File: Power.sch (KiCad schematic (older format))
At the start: 38 parts, among them J17 Power Input, Q4 YJS9435A, U6 A4403, U7 MCP16301

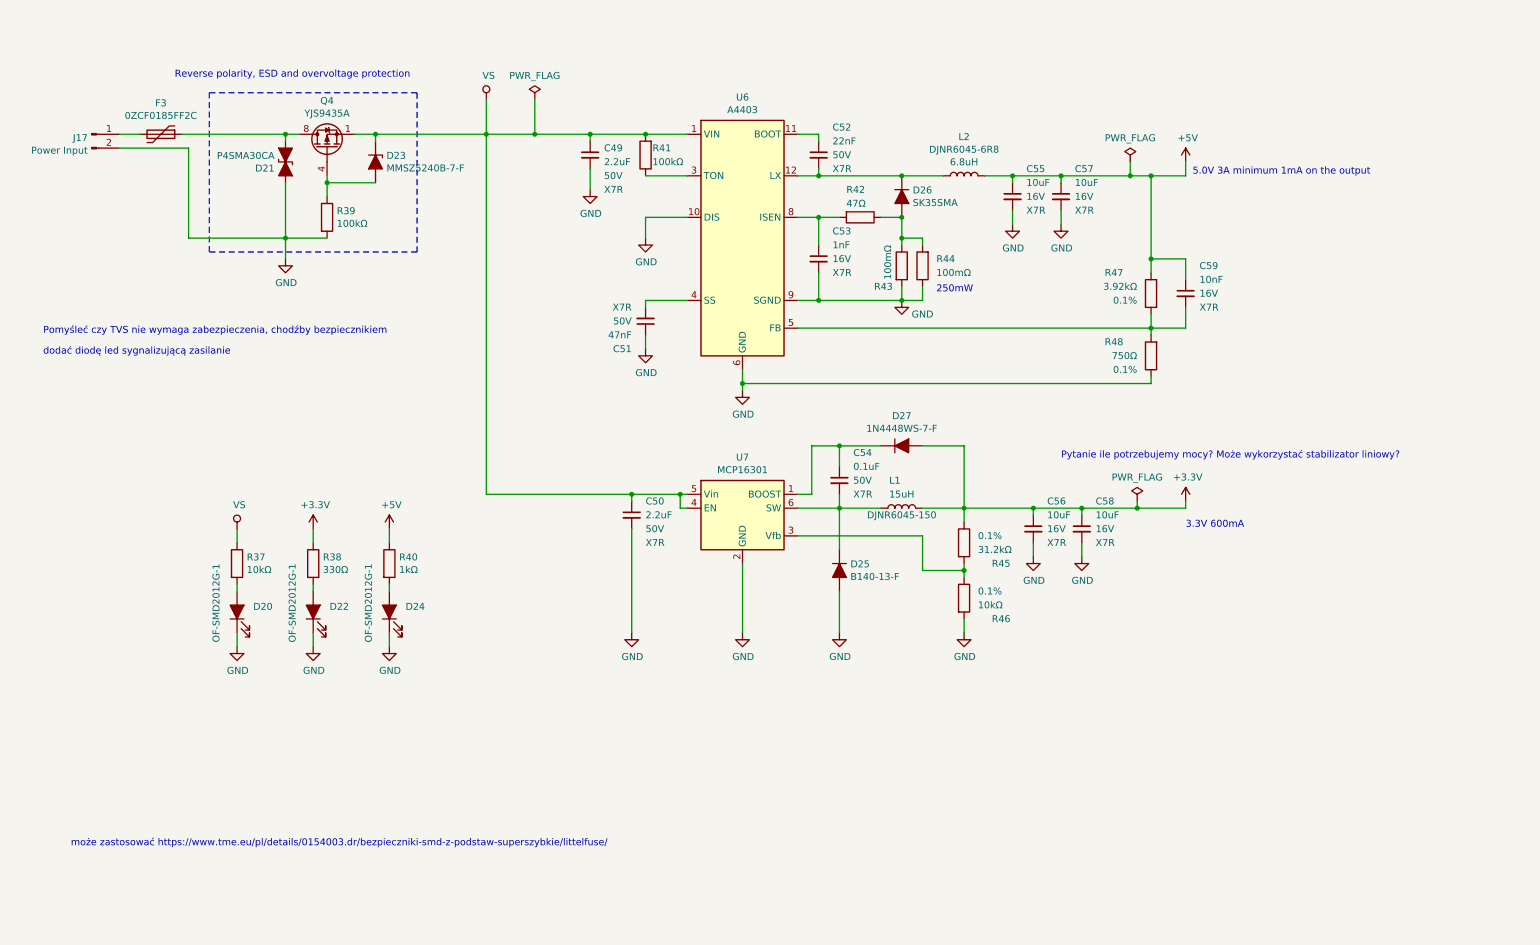
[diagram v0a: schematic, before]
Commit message: Added 12V regulator, aditional input, outputs, improved inputs ESD
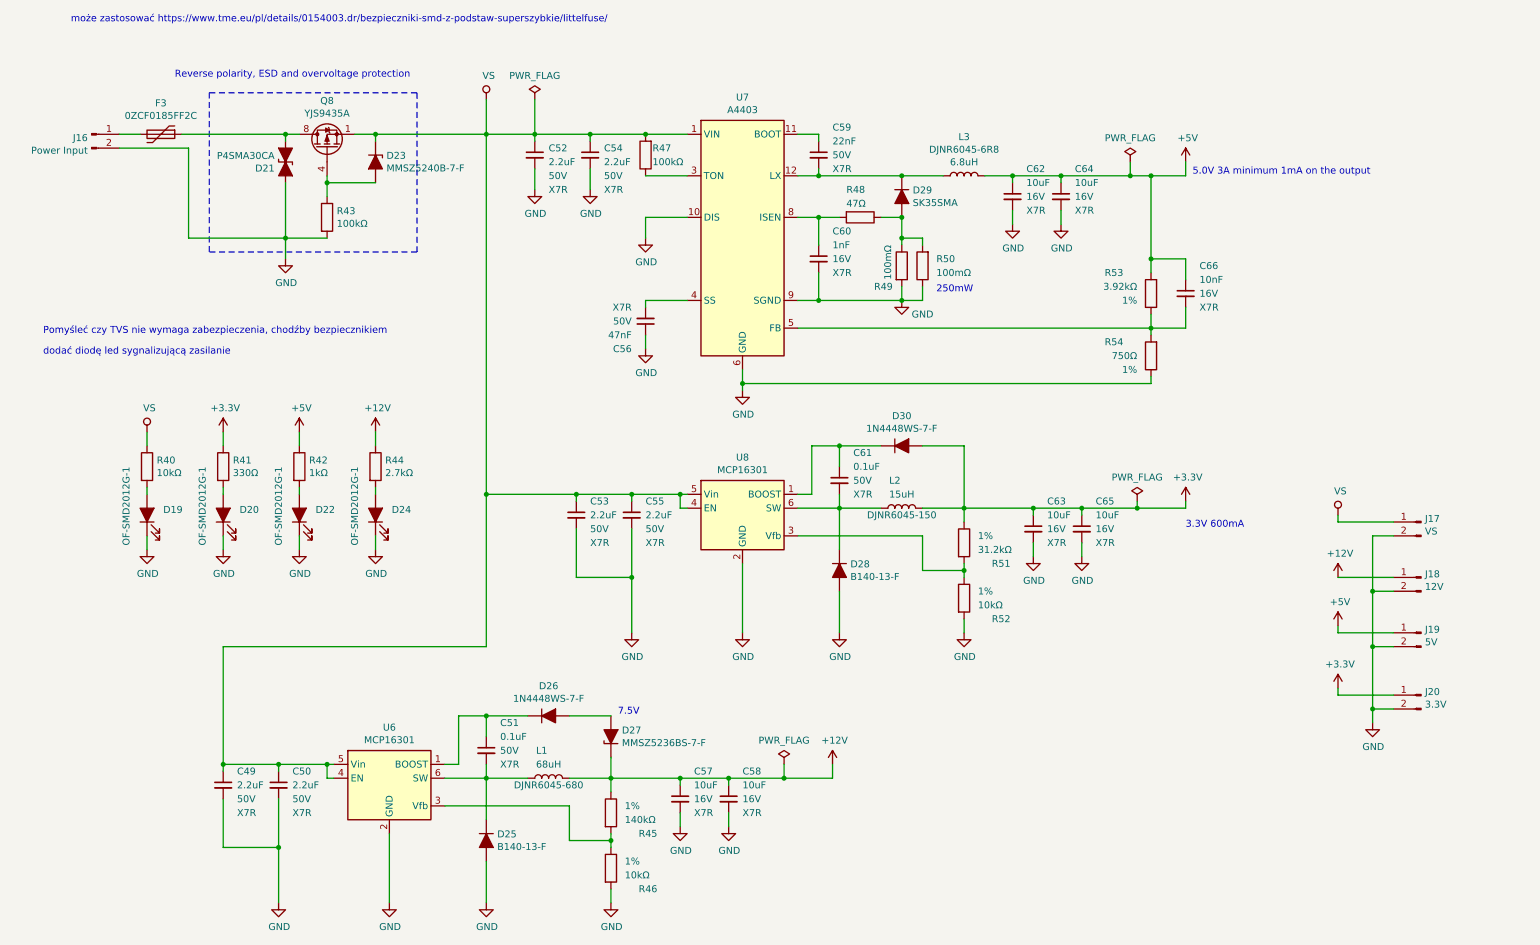
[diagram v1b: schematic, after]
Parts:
- added C49, C50, C52, C53: 2.2uF, Capacitor_SMD:C_1206_3216Metric, symbol Device:C_Small
- added C51: 0.1uF, Capacitor_SMD:C_0603_1608Metric, symbol Device:C_Small
- added C57, C58: 10uF, Capacitor_SMD:C_1206_3216Metric, symbol Device:C_Small
- added D24: OF-SMD2012G-1, Diode_SMD:D_0805_2012Metric, symbol Device:LED_ALT
- added D25: B140-13-F, Diode_SMD:D_SMA, symbol Device:D_ALT
- added D26: 1N4448WS-7-F, Diode_SMD:D_SOD-323, symbol Device:D_ALT
- added D27: MMSZ5236BS-7-F, Diode_SMD:D_SOD-323, symbol Device:D_Zener_ALT
- added J17: VS, Connector_JST:JST_PH_B2B-PH-K_1x02_P2.00mm_Vertical, symbol Connector:Conn_01x02_Male
- added J18: 12V, Connector_JST:JST_PH_B2B-PH-K_1x02_P2.00mm_Vertical, symbol Connector:Conn_01x02_Male
- added J19: 5V, Connector_JST:JST_PH_B2B-PH-K_1x02_P2.00mm_Vertical, symbol Connector:Conn_01x02_Male
- added J20: 3.3V, Connector_JST:JST_PH_B2B-PH-K_1x02_P2.00mm_Vertical, symbol Connector:Conn_01x02_Male
- added L1: DJNR6045-680, footprints:L_6.2x6.2_H4.5, symbol Device:L
- added R44: 2.7kΩ, Resistor_SMD:R_0603_1608Metric, symbol Device:R
- added R45: 140kΩ, Resistor_SMD:R_0603_1608Metric, symbol Device:R
- added R46: 10kΩ, Resistor_SMD:R_0603_1608Metric, symbol Device:R
- added U6: MCP16301, Package_TO_SOT_SMD:SOT-23-6, symbol Regulator_Switching:MCP16301
- R51: renamed from R45; Tolerancja 0.1% -> 1%
- R52: renamed from R46; Tolerancja 0.1% -> 1%
- R53: renamed from R47; Tolerancja 0.1% -> 1%
- R54: renamed from R48; Tolerancja 0.1% -> 1%
- renumbered C49 to C54, C50 to C55, C51 to C56, C52 to C59, C53 to C60, C54 to C61, C55 to C62, C56 to C63, C57 to C64, C58 to C65, C59 to C66, D20 to D19, D22 to D20, D24 to D22, D25 to D28, D26 to D29, D27 to D30, J17 to J16, L1 to L2, L2 to L3, Q4 to Q8, R37 to R40, R38 to R41, R40 to R42, R39 to R43, R41 to R47, R42 to R48, R43 to R49, R44 to R50, U6 to U7, U7 to U8
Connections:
- net +3V3: now also J20.1 (Pin_1)
- net +5V: now also J19.1 (Pin_1)
- net GND: now also C49.2, C50.2, C52.2, C53.2, C57.2, C58.2, D24.1 (K), D25.2 (A), J17.2 (Pin_2), J18.2 (Pin_2), J19.2 (Pin_2), J20.2 (Pin_2), R46.2, U6.2 (GND)
- net VS: now also C49.1, C50.1, C52.1, C53.1, J17.1 (Pin_1), U6.4 (EN), U6.5 (Vin)
- new net: C51.1, D26.1 (K), U6.1 (BOOST)
- new net: R45.2, R46.1, U6.3 (Vfb)
- new net: C51.2, D25.1 (K), L1.1, U6.6 (SW)
- new net: D26.2 (A), D27.2 (A)
- new net: D24.2 (A), R44.2
- new net +12V: C57.1, C58.1, D27.1 (K), J18.1 (Pin_1), L1.2, R44.1, R45.1
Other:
- note added: "7.5V"
- note removed: "Pytanie ile potrzebujemy mocy? Może wykorzystać stabilizator liniowy?"
- moved on the sheet: D19, D20, D22, R40, R41, R42

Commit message: Added analog input
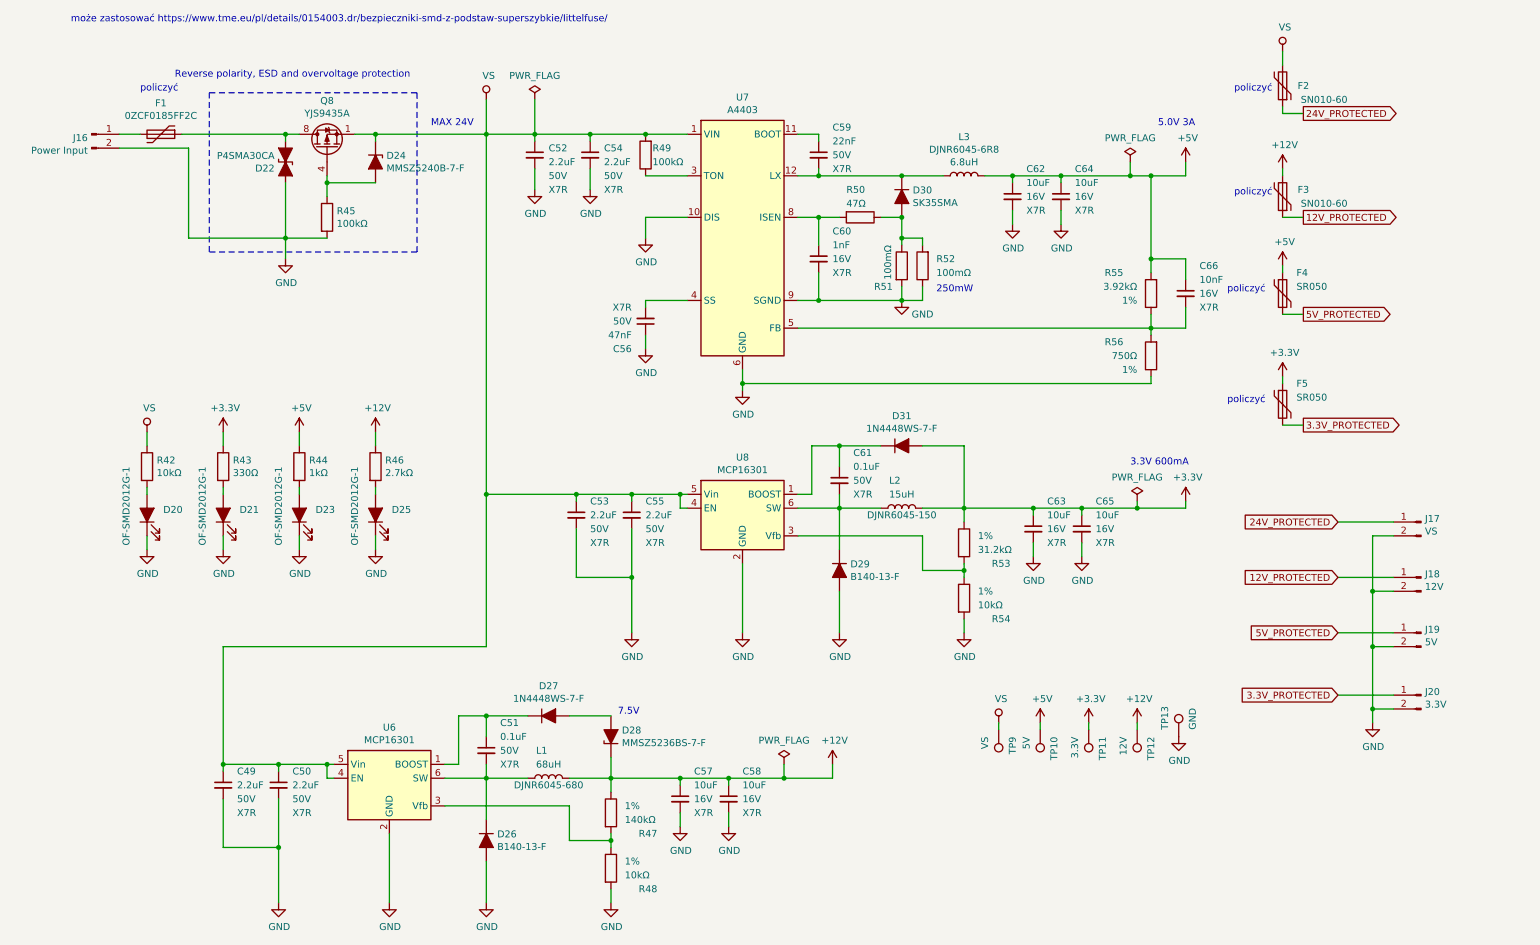
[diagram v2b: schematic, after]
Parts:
- added F2, F3: SN010-60, Fuse:Fuse_1206_3216Metric, symbol Device:Polyfuse
- added F4, F5: SR050, Fuse:Fuse_0805_2012Metric, symbol Device:Polyfuse
- added TP10: 5V, TestPoint:TestPoint_Pad_D1.5mm, symbol Connector:TestPoint
- added TP11: 3.3V, TestPoint:TestPoint_Pad_D1.5mm, symbol Connector:TestPoint
- added TP12: 12V, TestPoint:TestPoint_Pad_D1.5mm, symbol Connector:TestPoint
- added TP13: GND, TestPoint:TestPoint_Pad_D1.5mm, symbol Connector:TestPoint
- added TP9: VS, TestPoint:TestPoint_Pad_D1.5mm, symbol Connector:TestPoint
- renumbered D19 to D20, D20 to D21, D21 to D22, D22 to D23, D23 to D24, D24 to D25, D25 to D26, D26 to D27, D27 to D28, D28 to D29, D29 to D30, D30 to D31, F3 to F1, R40 to R42, R41 to R43, R42 to R44, R43 to R45, R44 to R46, R45 to R47, R46 to R48, R47 to R49, R48 to R50, R49 to R51, R50 to R52, R51 to R53, R52 to R54, R53 to R55, R54 to R56
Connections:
- net +12V: now also F3.2, TP12.1; no longer J18.1 (Pin_1)
- net +3V3: now also F5.1, TP11.1; no longer J20.1 (Pin_1)
- net +5V: now also F4.1, TP10.1; no longer J19.1 (Pin_1)
- net GND: now also TP13.1
- net VS: now also F2.2, TP9.1; no longer J17.1 (Pin_1)
- new net 12V_PROTECTED: F3.1, J18.1 (Pin_1)
- new net 24V_PROTECTED: F2.1, J17.1 (Pin_1)
- new net 3.3V_PROTECTED: F5.2, J20.1 (Pin_1)
- new net 5V_PROTECTED: F4.2, J19.1 (Pin_1)
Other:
- note added: "5.0V 3A"
- note added: "MAX 24V"
- note added: "policzyć"
- note removed: "5.0V 3A minimum 1mA on the output"
- note removed: "Pomyśleć czy TVS nie wymaga zabezpieczenia, chodźby bezpiecznikiem"
- note removed: "dodać diodę led sygnalizującą zasilanie"

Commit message: Improve ESD Protection for TMC2209, Fuses. Schematic ready v1
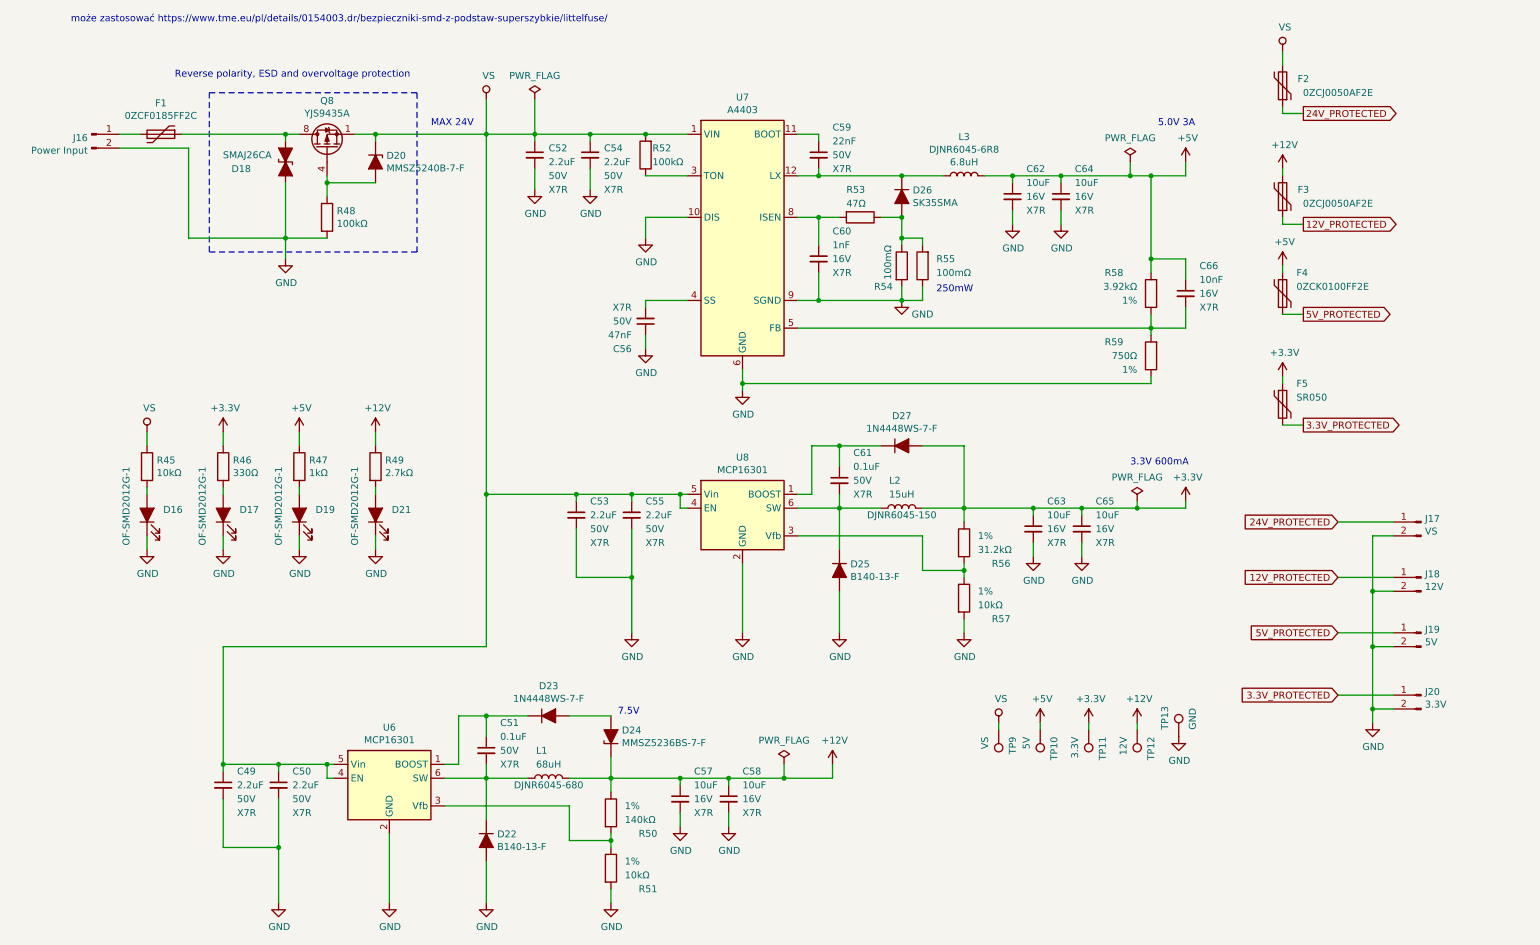
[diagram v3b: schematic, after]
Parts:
- removed D22: P4SMA30CA, Diode_SMD:D_SMA, symbol Device:D_TVS_ALT
- added D18: SMAJ26CA, Diode_SMD:D_SMA, symbol Device:D_TVS_ALT
- F2, F3: value SN010-60 -> 0ZCJ0050AF2E; Cena 0.3763 -> 0.6728; Link https://www.tme.eu/pl/details/sn010-60/bezpieczniki-polimer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 -> https://www.tme.eu/pl/details/0zcj0050af2e/bezpieczniki-pol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; Model SN010-60 -> 0ZCJ0050AF2E; Opis Bezpiecznik: polimerowy PTC; 100mA; Obud: 1206 -> Bezpiecznik: polimerowy PTC; 500mA; Imax: 100A; Obud: 1206;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; Producent ECE -> BEL FUSE
- F4: value SR050 -> 0ZCK0100FF2E; Cena 0.9060 -> 1.04; Link https://www.tme.eu/pl/details/sr050-06/bezpieczniki-polimer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 -> https://www.tme.eu/pl/details/0zck0100ff2e/bezpieczniki-pol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; Model SR050-06 -> 0ZCK0100FF2E; Opis Bezpiecznik: polimerowy PTC; 500mA; Obud: 0805 -> Bezpiecznik: polimerowy PTC; 1A; Imax: 40A; Obud: 0805; 0ZCK; Producent ECE -> BEL FUSE
- renumbered D20 to D16, D21 to D17, D23 to D19, D24 to D20, D25 to D21, D26 to D22, D27 to D23, D28 to D24, D29 to D25, D30 to D26, D31 to D27, R42 to R45, R43 to R46, R44 to R47, R45 to R48, R46 to R49, R47 to R50, R48 to R51, R49 to R52, R50 to R53, R51 to R54, R52 to R55, R53 to R56, R54 to R57, R55 to R58, R56 to R59
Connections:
- net GND: now also D18.1 (A1)
- net at F1.1, Q8.5 (D), Q8.6 (D)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: now also D18.2 (A2)
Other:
- note removed: "policzyć"

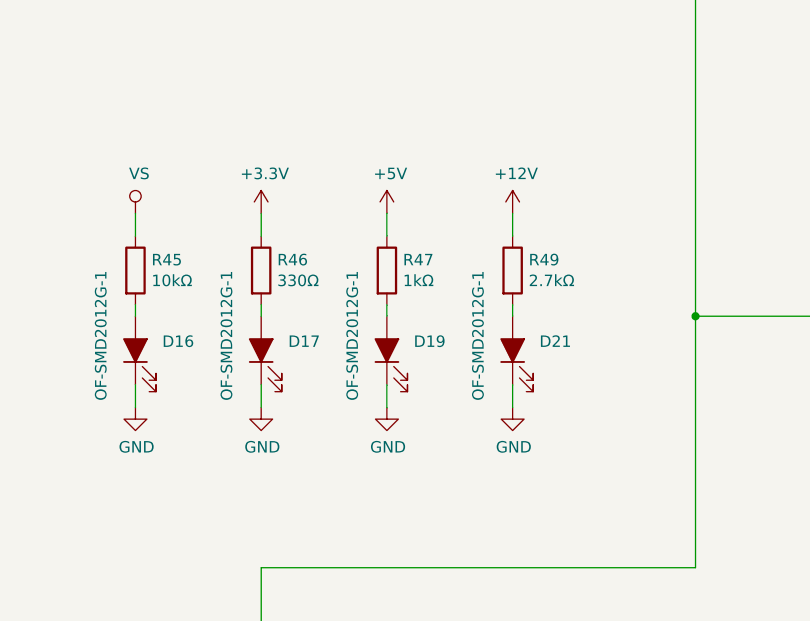
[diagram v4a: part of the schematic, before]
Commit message: Routing emergnency, photo barier, relay, voltage detect, analog, footprint improvment
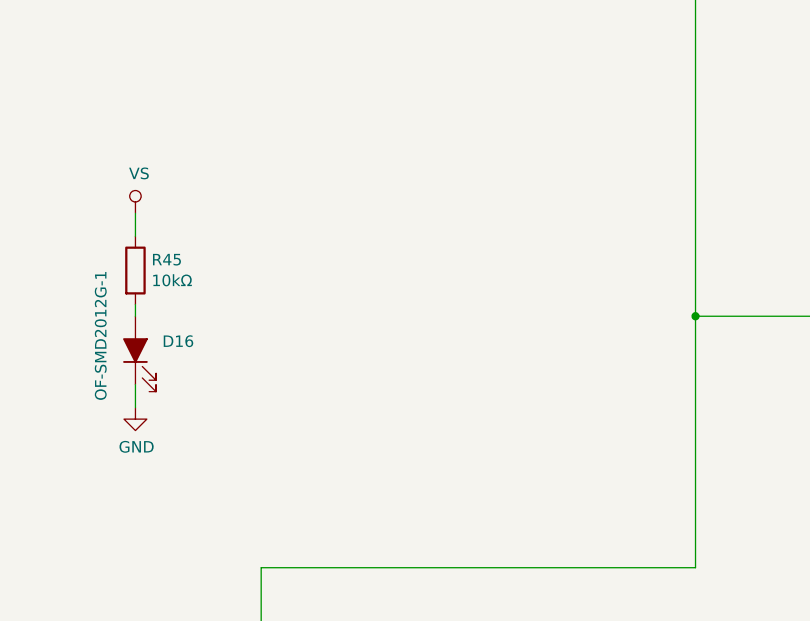
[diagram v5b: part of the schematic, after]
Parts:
- removed D17, D19, D21: OF-SMD2012G-1, Diode_SMD:D_0805_2012Metric, symbol Device:LED_ALT
- removed R46: 330Ω, Resistor_SMD:R_0603_1608Metric, symbol Device:R
- removed R47: 1kΩ, Resistor_SMD:R_0603_1608Metric, symbol Device:R
- removed R49: 2.7kΩ, Resistor_SMD:R_0603_1608Metric, symbol Device:R

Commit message: TMC2209 routing step 2/3
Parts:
- added C1, C15: 120uF, Capacitor_THT:CP_Radial_D8.0mm_P3.50mm, symbol Device:CP_Small
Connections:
- net GND: now also C1.2, C15.2
- net VS: now also C1.1, C15.1
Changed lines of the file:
@@
 	0    -1   -1   0
 $EndComp
+$Comp
+L Device:CP_Small C?
+U 1 1 5E284A7D
+P 2800 3800
+AR Path="/5DE588DC/5E284A7D" Ref="C?"  Part="1"
+AR Path="/5E1018C2/5E284A7D" Ref="C15"  Part="1"
+F 0 "C15" H 2888 3891 50  0000 L CNN
+F 1 "120uF" H 2888 3800 50  0000 L CNN
+F 2 "Capacitor_THT:CP_Radial_D8.0mm_P3.50mm" H 2800 3800 50  0001 C CNN
+F 3 "~" H 2800 3800 50  0001 C CNN
+F 4 "50V" H 2888 3709 50  0000 L CNN "Napięcie"
+F 5 "1.074" H 2800 3800 50  0001 C CNN "Cena"
+F 6 "EEUFR1H121L" H 2800 3800 50  0001 C CNN "Model"
+F 7 "Panasonic" H 2800 3800 50  0001 C CNN "Producent"
+F 8 "20%" H 2800 3800 50  0001 C CNN "Tolerancja"
+F 9 "THT" H 2800 3800 50  0001 C CNN "Typ"
+F 10 "https://www.tme.eu/pl/details/eeufr1h121l/kondensatory-elektr-tht-niskoimpedan/panasonic/" H 2800 3800 50  0001 C CNN "Link"
+F 11 "Kondensator: elektrolityczny; niskoimpedancyjny; THT; 120uF; ±20% " H 2800 3800 50  0001 C CNN "Opis"
+	1    2800 3800
+	1    0    0    -1
+$EndComp
+$Comp
+L Device:CP_Small C?
+U 1 1 5E2A7E64
+P 2400 3800
+AR Path="/5DE588DC/5E2A7E64" Ref="C?"  Part="1"
+AR Path="/5E1018C2/5E2A7E64" Ref="C1"  Part="1"
+F 0 "C1" H 2488 3891 50  0000 L CNN
+F 1 "120uF" H 2488 3800 50  0000 L CNN
+F 2 "Capacitor_THT:CP_Radial_D8.0mm_P3.50mm" H 2400 3800 50  0001 C CNN
+F 3 "~" H 2400 3800 50  0001 C CNN
+F 4 "50V" H 2488 3709 50  0000 L CNN "Napięcie"
+F 5 "1.074" H 2400 3800 50  0001 C CNN "Cena"
+F 6 "EEUFR1H121L" H 2400 3800 50  0001 C CNN "Model"
+F 7 "Panasonic" H 2400 3800 50  0001 C CNN "Producent"
+F 8 "20%" H 2400 3800 50  0001 C CNN "Tolerancja"
+F 9 "THT" H 2400 3800 50  0001 C CNN "Typ"
+F 10 "https://www.tme.eu/pl/details/eeufr1h121l/kondensatory-elektr-tht-niskoimpedan/panasonic/" H 2400 3800 50  0001 C CNN "Link"
+F 11 "Kondensator: elektrolityczny; niskoimpedancyjny; THT; 120uF; ±20% " H 2400 3800 50  0001 C CNN "Opis"
+	1    2400 3800
+	1    0    0    -1
+$EndComp
+$Comp
+L power:VS #PWR0104
+U 1 1 5E2A820A
+P 2400 3600
+F 0 "#PWR0104" H 2200 3450 50  0001 C CNN
+F 1 "VS" H 2417 3773 50  0000 C CNN
+F 2 "" H 2400 3600 50  0001 C CNN
+F 3 "" H 2400 3600 50  0001 C CNN
+	1    2400 3600
+	1    0    0    -1
+$EndComp
+$Comp
+L power:GND #PWR?
+U 1 1 5E2A862B
+P 2400 4000
+AR Path="/5DE588DC/5E2A862B" Ref="#PWR?"  Part="1"
+AR Path="/5DE587B9/5E2A862B" Ref="#PWR?"  Part="1"
+AR Path="/5E1018C2/5E2A862B" Ref="#PWR0105"  Part="1"
+F 0 "#PWR0105" H 2400 3750 50  0001 C CNN
+F 1 "GND" H 2405 3827 50  0000 C CNN
+F 2 "" H 2400 4000 50  0001 C CNN
+F 3 "" H 2400 4000 50  0001 C CNN
+	1    2400 4000
+	1    0    0    -1
+$EndComp
+Wire Wire Line
+	2400 3600 2400 3650
+Wire Wire Line
+	2400 3900 2400 3950
+Wire Wire Line
+	2400 3650 2800 3650
+Wire Wire Line
+	2800 3650 2800 3700
+Connection ~ 2400 3650
+Wire Wire Line
+	2400 3650 2400 3700
+Wire Wire Line
+	2400 3950 2800 3950
+Wire Wire Line
+	2800 3950 2800 3900
+Connection ~ 2400 3950
+Wire Wire Line
+	2400 3950 2400 4000
 $EndSCHEMATC
